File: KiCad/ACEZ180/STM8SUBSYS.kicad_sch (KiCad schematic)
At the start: 4 parts

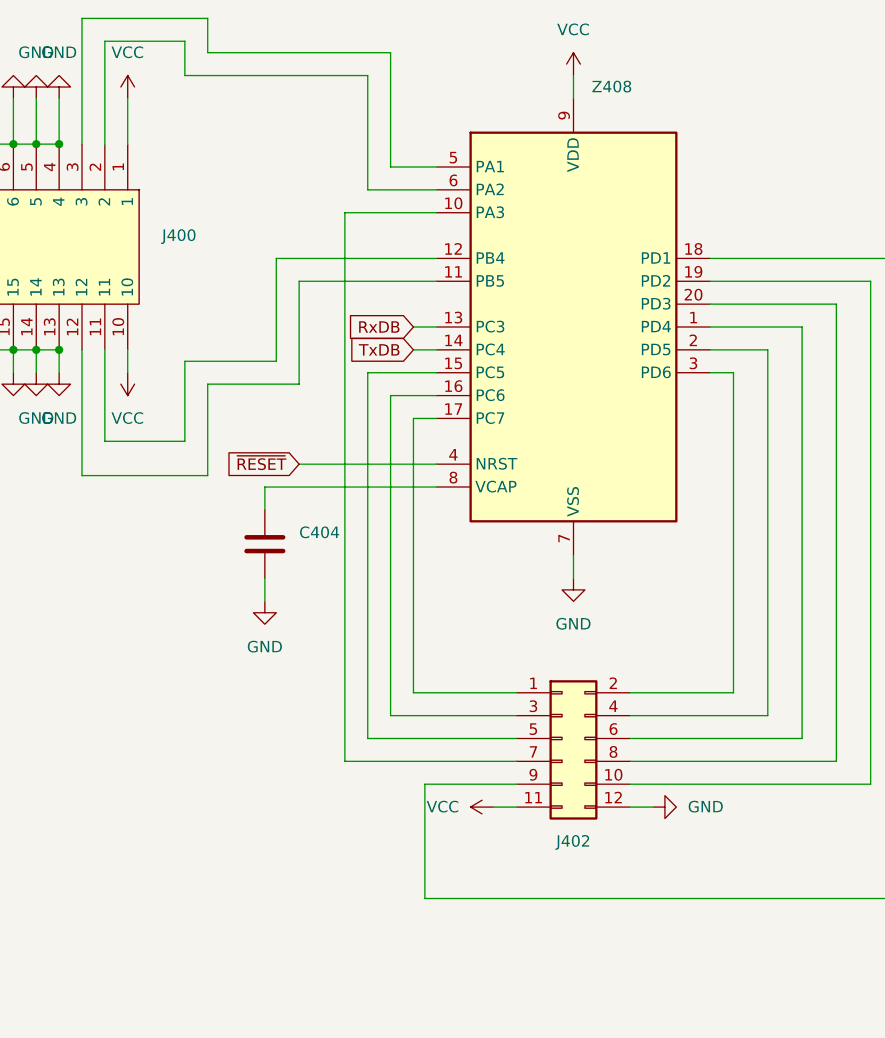
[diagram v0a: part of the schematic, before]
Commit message: Fix mistake with ROM Select.
Signed-off-by: John Bradley <flypie@rocketmail.com>
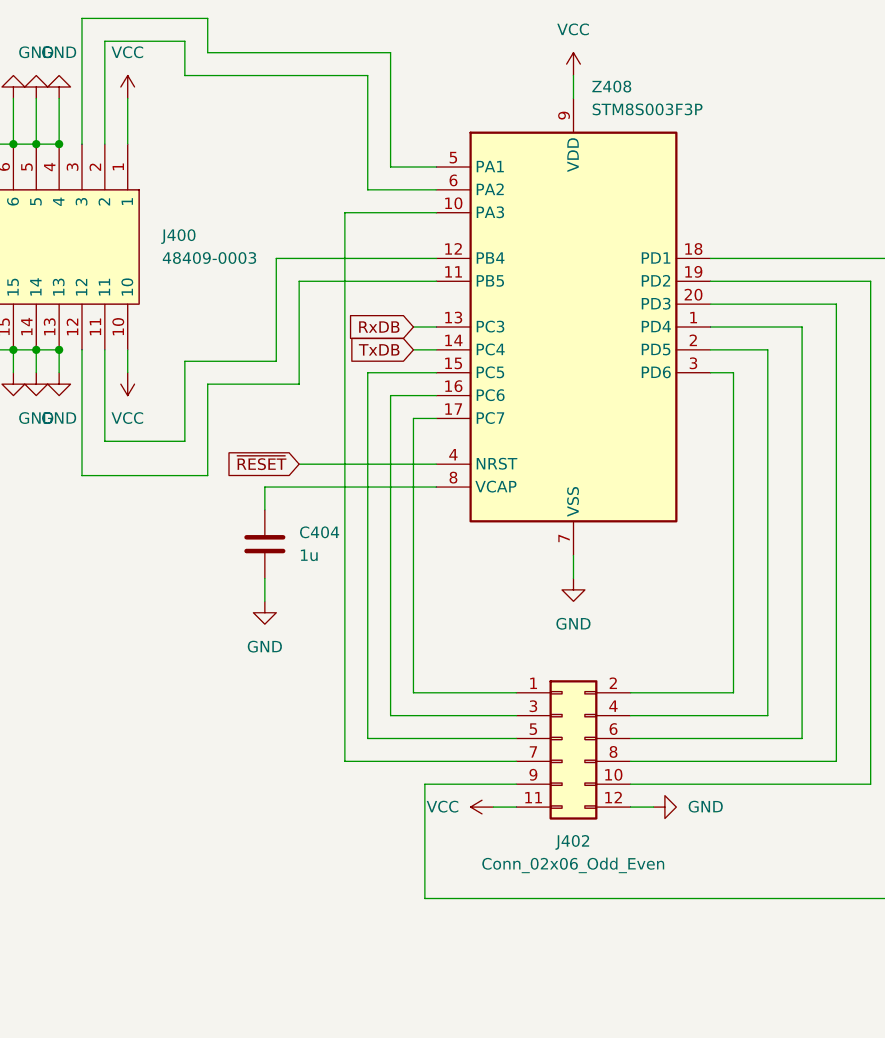
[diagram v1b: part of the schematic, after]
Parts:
- C404: value (none) -> 1u; footprint (none) -> Capacitor_THT:C_Disc_D3.0mm_W1.6mm_P2.50mm
- J400: value (none) -> 48409-0003; footprint (none) -> 48409-0003
- J402: value (none) -> Conn_02x06_Odd_Even; footprint (none) -> Connector_PinHeader_2.54mm:PinHeader_2x06_P2.54mm_Vertical
- Z408: value (none) -> STM8S003F3P; footprint (none) -> Package_SO:TSSOP-20_4.4x6.5mm_P0.65mm
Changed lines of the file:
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@@
       (effects (font (size 1.27 1.27)) (justify left))
     )
-    (property "Value" "" (id 1) (at 107.95 77.4699 90)
-      (effects (font (size 1.27 1.27)) (justify left))
-    )
-    (property "Footprint" "" (id 2) (at 107.95 97.155 0)
+    (property "Value" "48409-0003" (id 1) (at 107.95 77.4699 90)
+      (effects (font (size 1.27 1.27)) (justify left))
+    )
+    (property "Footprint" "48409-0003" (id 2) (at 107.95 97.155 0)
       (effects (font (size 1.27 1.27)) (justify left) hide)
     )
@@
       (effects (font (size 1.27 1.27)) (justify left))
     )
-    (property "Value" "" (id 1) (at 155.6894 60.96 0)
-      (effects (font (size 1.27 1.27)) (justify left))
-    )
-    (property "Footprint" "" (id 2) (at 154.94 57.15 0)
+    (property "Value" "STM8S003F3P" (id 1) (at 155.6894 60.96 0)
+      (effects (font (size 1.27 1.27)) (justify left))
+    )
+    (property "Footprint" "Package_SO:TSSOP-20_4.4x6.5mm_P0.65mm" (id 2) (at 154.94 57.15 0)
       (effects (font (size 1.27 1.27)) (justify left) hide)
     )
@@
     (in_bom yes) (on_board yes) (fields_autoplaced)
     (property "Reference" "J402" (id 0) (at 153.67 142.24 0))
-    (property "Value" "" (id 1) (at 153.67 144.78 0))
-    (property "Footprint" "" (id 2) (at 152.4 130.81 0)
+    (property "Value" "Conn_02x06_Odd_Even" (id 1) (at 153.67 144.78 0))
+    (property "Footprint" "Connector_PinHeader_2.54mm:PinHeader_2x06_P2.54mm_Vertical" (id 2) (at 152.4 130.81 0)
       (effects (font (size 1.27 1.27)) hide)
     )
@@
       (effects (font (size 1.27 1.27)) (justify left))
     )
-    (property "Value" "" (id 1) (at 123.19 110.4899 0)
-      (effects (font (size 1.27 1.27)) (justify left))
-    )
-    (property "Footprint" "" (id 2) (at 119.38 109.22 0)
-      (effects (font (size 1.27 1.27)) hide)
-    )
+    (property "Value" "1u" (id 1) (at 123.19 110.4899 0)
+      (effects (font (size 1.27 1.27)) (justify left))
+    )
+    (property "Footprint" "Capacitor_THT:C_Disc_D3.0mm_W1.6mm_P2.50mm" (id 2) (at 119.38 109.22 0)
+      (effects (font (size 1.27 1.27)) hide)
+    )
